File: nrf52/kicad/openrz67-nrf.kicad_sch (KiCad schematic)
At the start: 13 parts, among them J1 Camera, J2 SWD, SW1 B3U-1000P, U1 E73-2G4M08S1C, U2 TLP172AM, U3 TLP172AM

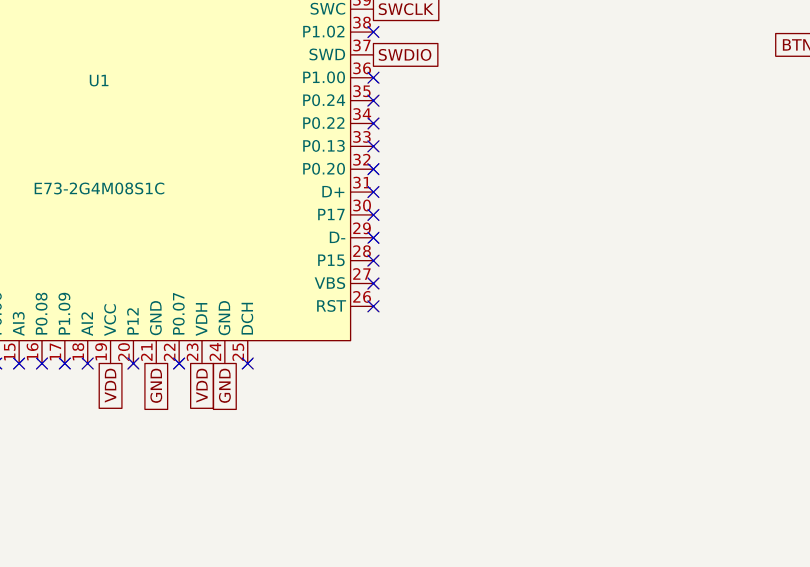
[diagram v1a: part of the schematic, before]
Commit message: nrf52: no paste on cell pad, VBUS to GND, vias out of pads
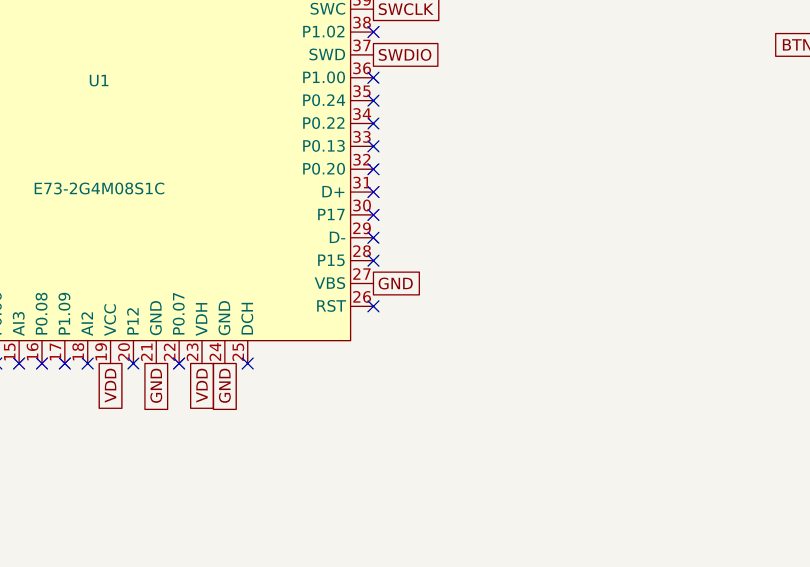
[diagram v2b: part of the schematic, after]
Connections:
- net GND: now also U1.27 (VBS)
- no-connect marks 35 -> 34
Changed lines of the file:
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@@
     (effects (font (size 1.27 1.27)) (justify right))
+  )
+  (global_label "GND" (shape passive) (at 90.48 106.51 0) (fields_autoplaced yes)
+    (effects (font (size 1.27 1.27)) (justify left))
   )
   (global_label "SWDIO" (shape passive) (at 90.48 81.11 0) (fields_autoplaced yes)
@@
   (no_connect (at 76.51 115.4))
   (no_connect (at 90.48 109.05))
-  (no_connect (at 90.48 106.51))
   (no_connect (at 90.48 103.97))
   (no_connect (at 90.48 101.43))

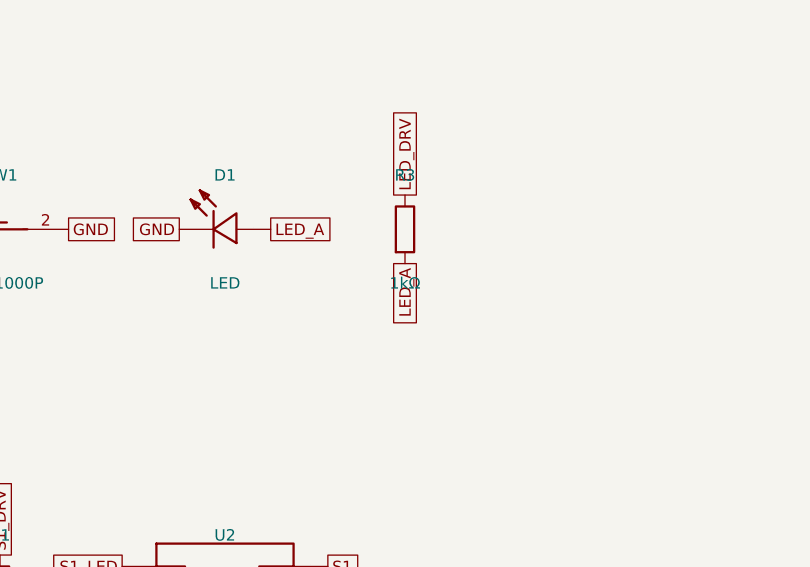
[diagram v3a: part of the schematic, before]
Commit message: nrf52 pcb: basic C2, R3 shares the 330 Ω part
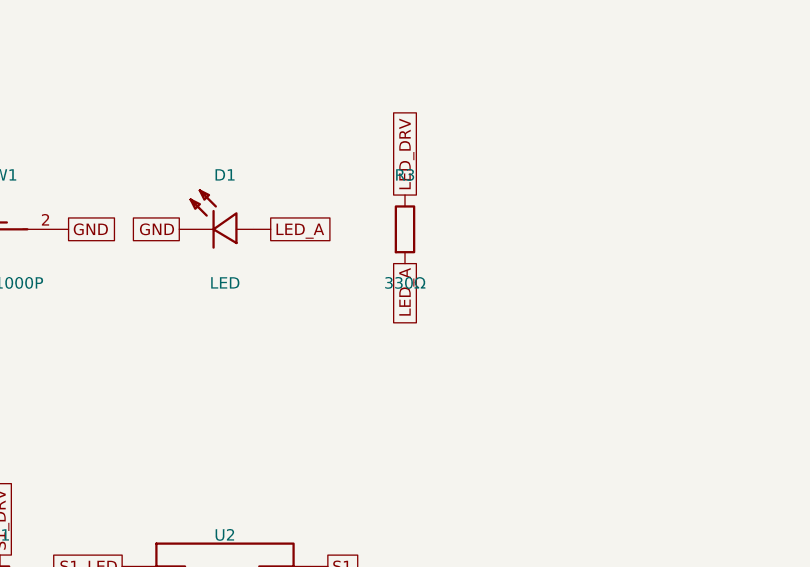
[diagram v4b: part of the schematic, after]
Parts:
- C2: LCSC C77020 -> C1525; MPN GRM155R71H104KE14D -> CL05B104KO5NNNC; Manufacturer muRata -> Samsung
- R3: value 1kΩ -> 330Ω; LCSC C11702 -> C25104; MPN 0402WGF1001TCE -> 0402WGF3300TCE
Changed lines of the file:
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@@
       (effects (font (size 1.27 1.27)))
     )
-    (property "Value" "1kΩ" (at 195 86 0)
+    (property "Value" "330Ω" (at 195 86 0)
       (effects (font (size 1.27 1.27)))
     )
@@
       (effects (font (size 1.27 1.27)) hide)
     )
-    (property "Description" "status LED series" (at 195 80 0)
+    (property "Description" "status LED series, same part as R1/R2" (at 195 80 0)
       (effects (font (size 1.27 1.27)) hide)
     )
-    (property "LCSC" "C11702" (at 195 80 0)
+    (property "LCSC" "C25104" (at 195 80 0)
       (effects (font (size 1.27 1.27)) hide)
     )
-    (property "MPN" "0402WGF1001TCE" (at 195 80 0)
+    (property "MPN" "0402WGF3300TCE" (at 195 80 0)
       (effects (font (size 1.27 1.27)) hide)
     )
@@
       (effects (font (size 1.27 1.27)) hide)
     )
-    (property "LCSC" "C77020" (at 195 40 0)
+    (property "LCSC" "C1525" (at 195 40 0)
       (effects (font (size 1.27 1.27)) hide)
     )
-    (property "MPN" "GRM155R71H104KE14D" (at 195 40 0)
+    (property "MPN" "CL05B104KO5NNNC" (at 195 40 0)
       (effects (font (size 1.27 1.27)) hide)
     )
-    (property "Manufacturer" "muRata" (at 195 40 0)
+    (property "Manufacturer" "Samsung" (at 195 40 0)
       (effects (font (size 1.27 1.27)) hide)
     )

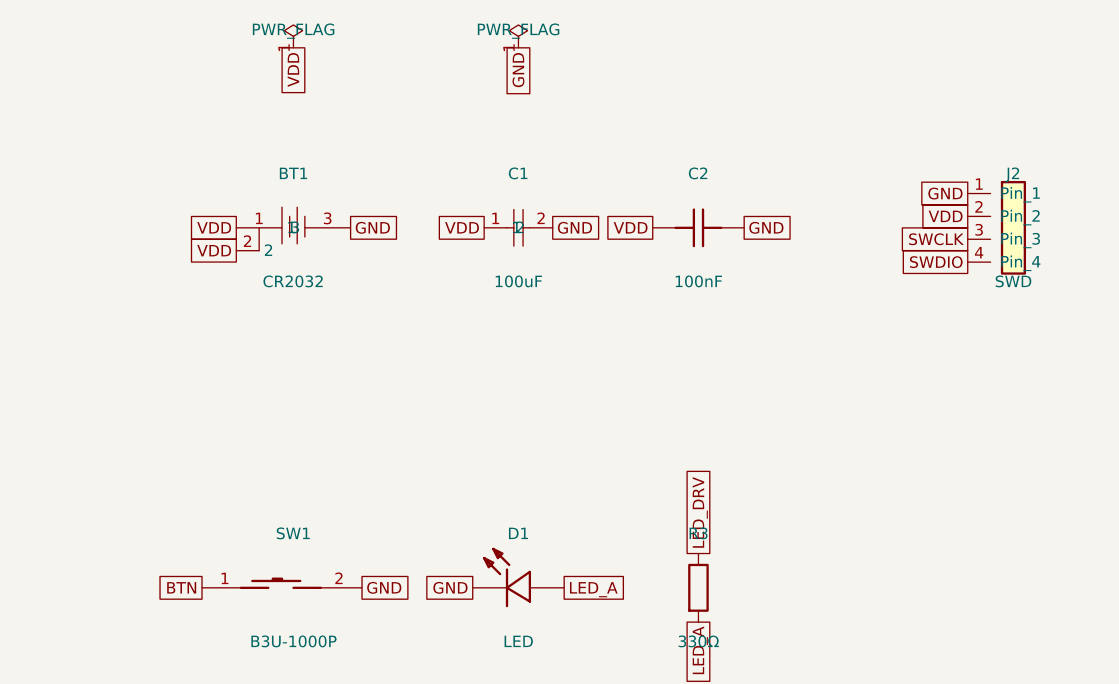
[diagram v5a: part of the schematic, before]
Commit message: nrf52 pcb: reverse-cell P-MOSFET
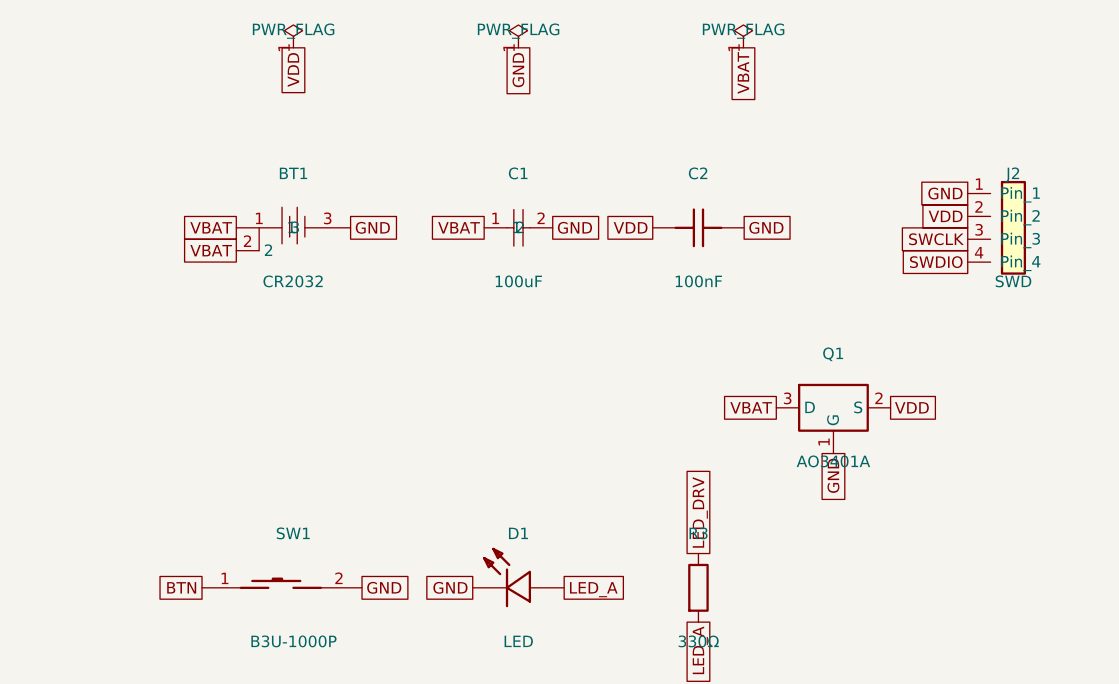
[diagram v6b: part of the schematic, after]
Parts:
- added Q1: AO3401A, openrz67-nrf:SOT-23, symbol openrz67-nrf:AO3401A
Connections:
- net GND: now also Q1.1 (G)
- net VDD: now also Q1.2 (S); no longer BT1.1, BT1.2, C1.1
- new net VBAT: BT1.1, BT1.2, C1.1, Q1.3 (D)
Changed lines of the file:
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@@
       (effects (font (size 1.27 1.27)) hide)
     )
-    (property "Description" "cell bulk at the clip terminal, carries radio and LED peaks" (at 175 40 0)
+    (property "Description" "cell bulk at the clip terminal, ahead of Q1 (ceramic, a reversed cell does not hurt it)" (at 175 40 0)
       (effects (font (size 1.27 1.27)) hide)
     )
@@
     (instances
       (project "openrz67-nrf" (path "/5d1c1d2e-0a3b-4c4d-9e5f-6a7b8c9d0e1f" (reference "C2") (unit 1)))
+    )
+  )
+  (symbol (lib_id "openrz67-nrf:AO3401A") (at 210 60 0) (unit 1)
+    (in_bom yes) (on_board yes) (dnp no)
+    (property "Reference" "Q1" (at 210 54 0)
+      (effects (font (size 1.27 1.27)))
+    )
+    (property "Value" "AO3401A" (at 210 66 0)
+      (effects (font (size 1.27 1.27)))
+    )
+    (property "Footprint" "openrz67-nrf:SOT-23" (at 210 60 0)
+      (effects (font (size 1.27 1.27)) hide)
+    )
+    (property "Datasheet" "" (at 210 60 0)
+      (effects (font (size 1.27 1.27)) hide)
+    )
+    (property "Description" "reverse-cell block: D on the clip, S on VDD, G on GND" (at 210 60 0)
+      (effects (font (size 1.27 1.27)) hide)
+    )
+    (property "LCSC" "C15127" (at 210 60 0)
+      (effects (font (size 1.27 1.27)) hide)
+    )
+    (property "MPN" "AO3401A" (at 210 60 0)
+      (effects (font (size 1.27 1.27)) hide)
+    )
+    (property "Manufacturer" "Alpha & Omega Semicon" (at 210 60 0)
+      (effects (font (size 1.27 1.27)) hide)
+    )
+    (pin "1")
+    (pin "2")
+    (pin "3")
+    (instances
+      (project "openrz67-nrf" (path "/5d1c1d2e-0a3b-4c4d-9e5f-6a7b8c9d0e1f" (reference "Q1") (unit 1)))
     )
   )
@@
     (instances (project "openrz67-nrf" (path "/5d1c1d2e-0a3b-4c4d-9e5f-6a7b8c9d0e1f" (reference "#FLG2") (unit 1))))
   )
+  (symbol (lib_id "openrz67-nrf:PWR_FLAG") (at 200 20 0) (unit 1)
+    (in_bom no) (on_board no) (dnp no)
+    (property "Reference" "#FLG3" (at 200 16 0) (effects (font (size 1.27 1.27)) hide))
+    (property "Value" "PWR_FLAG" (at 200 18 0) (effects (font (size 1.27 1.27))))
+    (property "Footprint" "" (at 200 20 0) (effects (font (size 1.27 1.27)) hide))
+    (property "Datasheet" "" (at 200 20 0) (effects (font (size 1.27 1.27)) hide))
+    (pin "1")
+    (instances (project "openrz67-nrf" (path "/5d1c1d2e-0a3b-4c4d-9e5f-6a7b8c9d0e1f" (reference "#FLG3") (unit 1))))
+  )
   (global_label "GND" (shape passive) (at 30.79 87.46 180) (fields_autoplaced yes)
     (effects (font (size 1.27 1.27)) (justify right))
@@
     (effects (font (size 1.27 1.27)) (justify left))
   )
-  (global_label "VDD" (shape passive) (at 143.65 40.0 180) (fields_autoplaced yes)
-    (effects (font (size 1.27 1.27)) (justify right))
-  )
-  (global_label "VDD" (shape passive) (at 143.65 42.54 180) (fields_autoplaced yes)
+  (global_label "VBAT" (shape passive) (at 143.65 40.0 180) (fields_autoplaced yes)
+    (effects (font (size 1.27 1.27)) (justify right))
+  )
+  (global_label "VBAT" (shape passive) (at 143.65 42.54 180) (fields_autoplaced yes)
     (effects (font (size 1.27 1.27)) (justify right))
   )
@@
     (effects (font (size 1.27 1.27)) (justify right))
   )
-  (global_label "VDD" (shape passive) (at 171.19 40.0 180) (fields_autoplaced yes)
+  (global_label "VBAT" (shape passive) (at 171.19 40.0 180) (fields_autoplaced yes)
     (effects (font (size 1.27 1.27)) (justify right))
   )
@@
     (effects (font (size 1.27 1.27)) (justify left))
   )
+  (global_label "GND" (shape passive) (at 210.0 65.08 270) (fields_autoplaced yes)
+    (effects (font (size 1.27 1.27)) (justify right))
+  )
+  (global_label "VDD" (shape passive) (at 216.35 60.0 0) (fields_autoplaced yes)
+    (effects (font (size 1.27 1.27)) (justify left))
+  )
+  (global_label "VBAT" (shape passive) (at 203.65 60.0 180) (fields_autoplaced yes)
+    (effects (font (size 1.27 1.27)) (justify right))
+  )
   (global_label "GND" (shape passive) (at 224.92 36.19 180) (fields_autoplaced yes)
     (effects (font (size 1.27 1.27)) (justify right))
@@
     (effects (font (size 1.27 1.27)) (justify right))
   )
+  (global_label "VBAT" (shape passive) (at 200 20 270) (fields_autoplaced yes)
+    (effects (font (size 1.27 1.27)) (justify right))
+  )

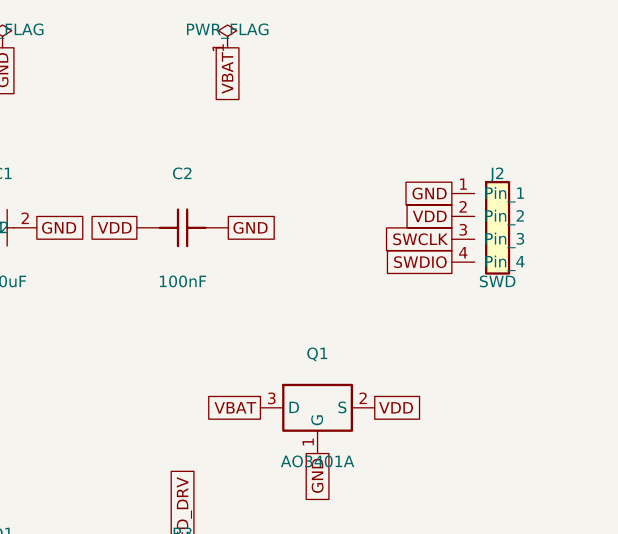
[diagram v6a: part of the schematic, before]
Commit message: nrf52: J2 mouth at the board edge, board 29.5 wide
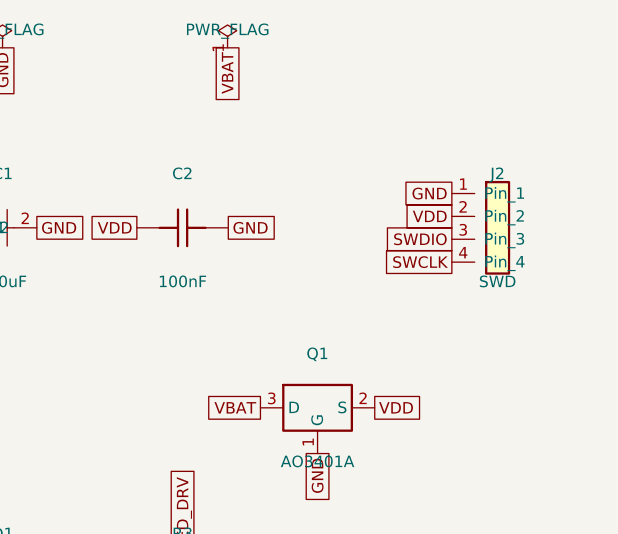
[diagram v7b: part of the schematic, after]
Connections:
- net SWCLK: now also J2.4 (Pin_4); no longer J2.3 (Pin_3)
- net SWDIO: now also J2.3 (Pin_3); no longer J2.4 (Pin_4)
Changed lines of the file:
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@@
       (effects (font (size 1.27 1.27)) hide)
     )
-    (property "Description" "SWD, SH 1.0 mm side-entry (Qwiic cable to the probe): 1 GND, 2 VDD, 3 SWCLK, 4 SWDIO" (at 230 40 0)
+    (property "Description" "SWD, SH 1.0 mm side-entry (Qwiic cable to the probe): 1 GND, 2 VDD, 3 SWDIO, 4 SWCLK" (at 230 40 0)
       (effects (font (size 1.27 1.27)) hide)
     )
@@
     (effects (font (size 1.27 1.27)) (justify right))
   )
-  (global_label "SWCLK" (shape passive) (at 224.92 41.27 180) (fields_autoplaced yes)
-    (effects (font (size 1.27 1.27)) (justify right))
-  )
-  (global_label "SWDIO" (shape passive) (at 224.92 43.81 180) (fields_autoplaced yes)
-    (effects (font (size 1.27 1.27)) (justify right))
-  )
+  (global_label "SWDIO" (shape passive) (at 224.92 41.27 180) (fields_autoplaced yes)
+    (effects (font (size 1.27 1.27)) (justify right))
+  )
+  (global_label "SWCLK" (shape passive) (at 224.92 43.81 180) (fields_autoplaced yes)
+    (effects (font (size 1.27 1.27)) (justify right))
+  )
